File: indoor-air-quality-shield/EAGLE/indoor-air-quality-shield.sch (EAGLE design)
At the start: 36 parts, among them J4 POWER_JACKSLT, Q1 MMBT2222A, U6 AP1509-50SG-13

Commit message: upadted pcb layout
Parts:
- removed J4: POWER_JACKSLT, Spark:POWER_JACKSLT
- removed JP5: M02PTH3, SparkFun-Connectors:M02PTH3
- removed R13: 1K, SparkFun-Passives:RESISTOR0603-RES
- removed R14, R15: (no value), pot:TRIM_US-RJ9W
- added J3: (no value), Connector:TWIG-4P-2.0-2.0
- added JP2: (no value), SparkFun-Connectors:M03PTH
- added R7, R8, R9: 1K, SparkFun-Passives:RESISTOR0603-RES
- D1: value LED-RGB-CC-THRUCLEAR -> B230; device SparkFun-LED:LED-RGB-CC-THRUCLEAR -> adafruit:DIODESMA
- D3: value B230 -> LED-RGB-CC-THRUCLEAR; device adafruit:DIODESMA -> SparkFun-LED:LED-RGB-CC-THRUCLEAR
- J1: value (none) -> POWER_JACKSLT; device Connector:TWIG-4P-2.0-2.0 -> Spark:POWER_JACKSLT
- JP1: value (none) -> M02PTH3; device SparkFun-Connectors:M03PTH -> SparkFun-Connectors:M02PTH3
- R1, R2, R3, R4: value (none) -> 50K; device SparkFun-Passives:RESISTOR0603-RES -> pot:TRIM_US-RJ9W
- R10: value (none) -> 10K
- R11, R12: value (none) -> 10K; device pot:TRIM_US-RJ9W -> SparkFun-Passives:RESISTOR0603-RES
- R5, R6: value (none) -> 1K
- U$1: value SPARK_CORE -> MQ_SENSOR_SOCKET; device Spark:SPARK_CORE -> Spark:MQ_SENSOR_SOCKET
- U$3: value MICS5525 -> MQ_SENSOR_SOCKET; device Spark:MICS5525 -> Spark:MQ_SENSOR_SOCKET
- U$4: value MQ_SENSOR_SOCKET -> MICS5525; device Spark:MQ_SENSOR_SOCKET -> Spark:MICS5525
- U$5: value MQ_SENSOR_SOCKET -> DHT22; device Spark:MQ_SENSOR_SOCKET -> Spark:DHT22
- U$6: value DHT22 -> SPARK_CORE; device Spark:DHT22 -> Spark:SPARK_CORE
- renumbered C10 to C2, C8 to C3, C9 to C1, LED5 to LED1, R16 to R10, U6 to U1
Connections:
- net +3V3: now also U$5.VDD, U$6.3V3; no longer U$1.3V3, U$6.VDD
- net +5V: now also J3.3, R11.2, R12.2, U$1.A1, U$1.A2, U$1.H+, U$3.A1, U$3.A2, U$4.S+, U$6.VIN; no longer J1.3, R13.2, R4.2, U$1.VIN, U$3.S+, U$4.A1, U$4.A2, U$5.A1, U$5.A2, U$5.H+
- net BLUE: now also R7.2, U$6.A7; no longer R3.2, U$1.A7
- net BTN1: now also U$6.D3; no longer U$1.D3
- net BTN2: now also U$6.D4; no longer U$1.D4
- net BUZZER: now also U$6.A4
- net DHT22: now also U$5.DATA, U$6.D2; no longer U$1.D2, U$6.DATA
- net GND: now also D3.CATHODE, J1.GND, J1.GNDBREAK, J3.4, JP2.1, R1.A, R1.S, R2.A, R2.S, R3.A, R3.S, R4.A, R4.S, U$4.H-, U$5.GND, U$6.GND@2, U$6.GND@21; no longer D1.CATHODE, J1.4, J4.GND, J4.GNDBREAK, JP5.1, R11.A, R11.S, R12.A, R12.S, R14.A, R14.S, R15.A, R15.S, U$1.GND@2, U$1.GND@21, U$3.H-, U$6.GND
- net GREEN: now also R8.2, U$6.A6; no longer R2.2, U$1.A6
- net MICS: now also R3.E, U$4.S-, U$6.A1; no longer R12.E, U$1.A1, U$3.S-
- net MQ1: now also R2.E, U$1.B1, U$1.B2, U$6.A2; no longer R14.E, U$1.A2, U$4.B1, U$4.B2
- net MQ2: now also R4.E, U$3.B1, U$3.B2, U$6.A3; no longer R15.E, U$1.A3, U$5.B1, U$5.B2
- net N$1: now also D3.BLUE_CATHODE, R7.1; no longer D1.BLUE_CATHODE, R3.1
- net N$14: now also D1.C; no longer D3.C
- net N$16: now also R5.1; no longer R13.1
- net N$2: now also D3.GREEN_CATHODE, R8.1; no longer D1.GREEN_CATHODE, R2.1
- net N$3: now also D3.RED_CATHODE, R9.1; no longer D1.RED_CATHODE, R1.1
- net N$32: now also D1.A, J1.PWR, JP1.2; no longer D3.A, J4.PWR, JP5.2
- net RED: now also R9.2, U$6.A5; no longer R1.2, U$1.A5
- net SCL: now also J3.1, R11.1, U$6.D1; no longer J1.1, R4.1, U$1.D1
- net SDA: now also J3.2, R12.1, U$6.D0; no longer J1.2, R5.1, U$1.D0
- net TGS: now also R1.E, U$6.A0; no longer R11.E, U$1.A0
- net UART_RX: now also JP2.3, U$6.RX; no longer JP1.3, U$1.RX
- net UART_TX: now also JP2.2, U$6.TX; no longer JP1.2, U$1.TX
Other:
- moved on the sheet: R5

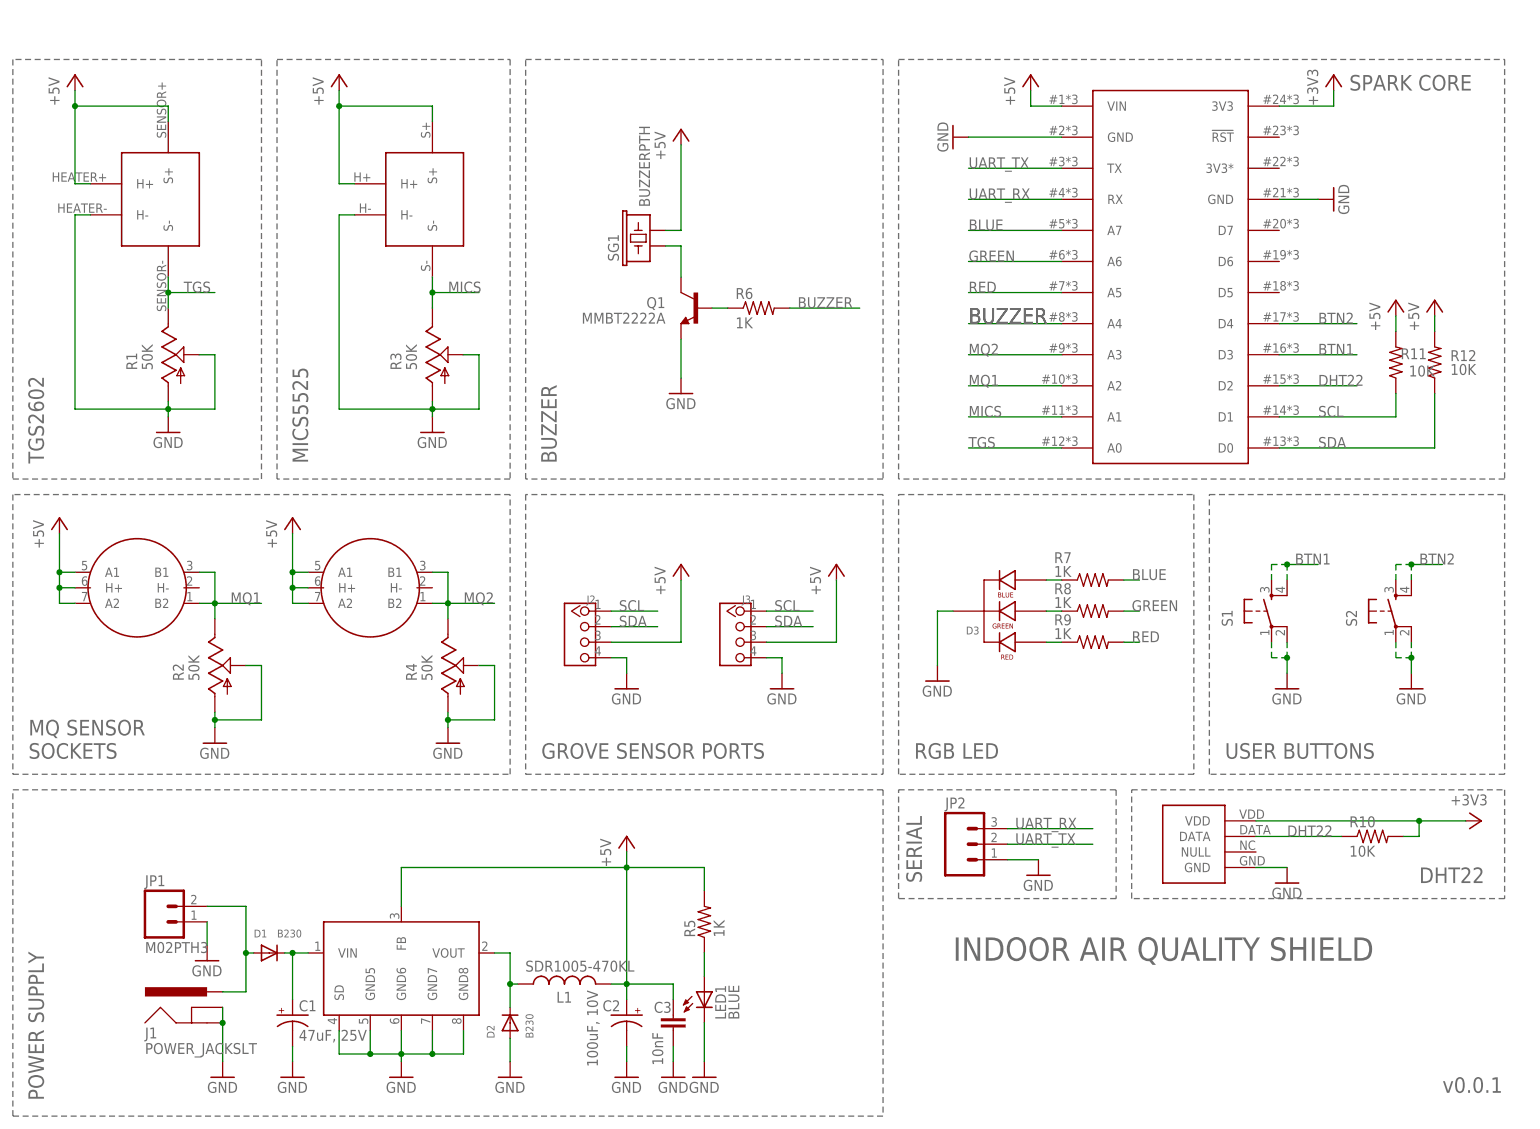
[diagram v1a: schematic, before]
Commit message: layed out indoor air quality pcb
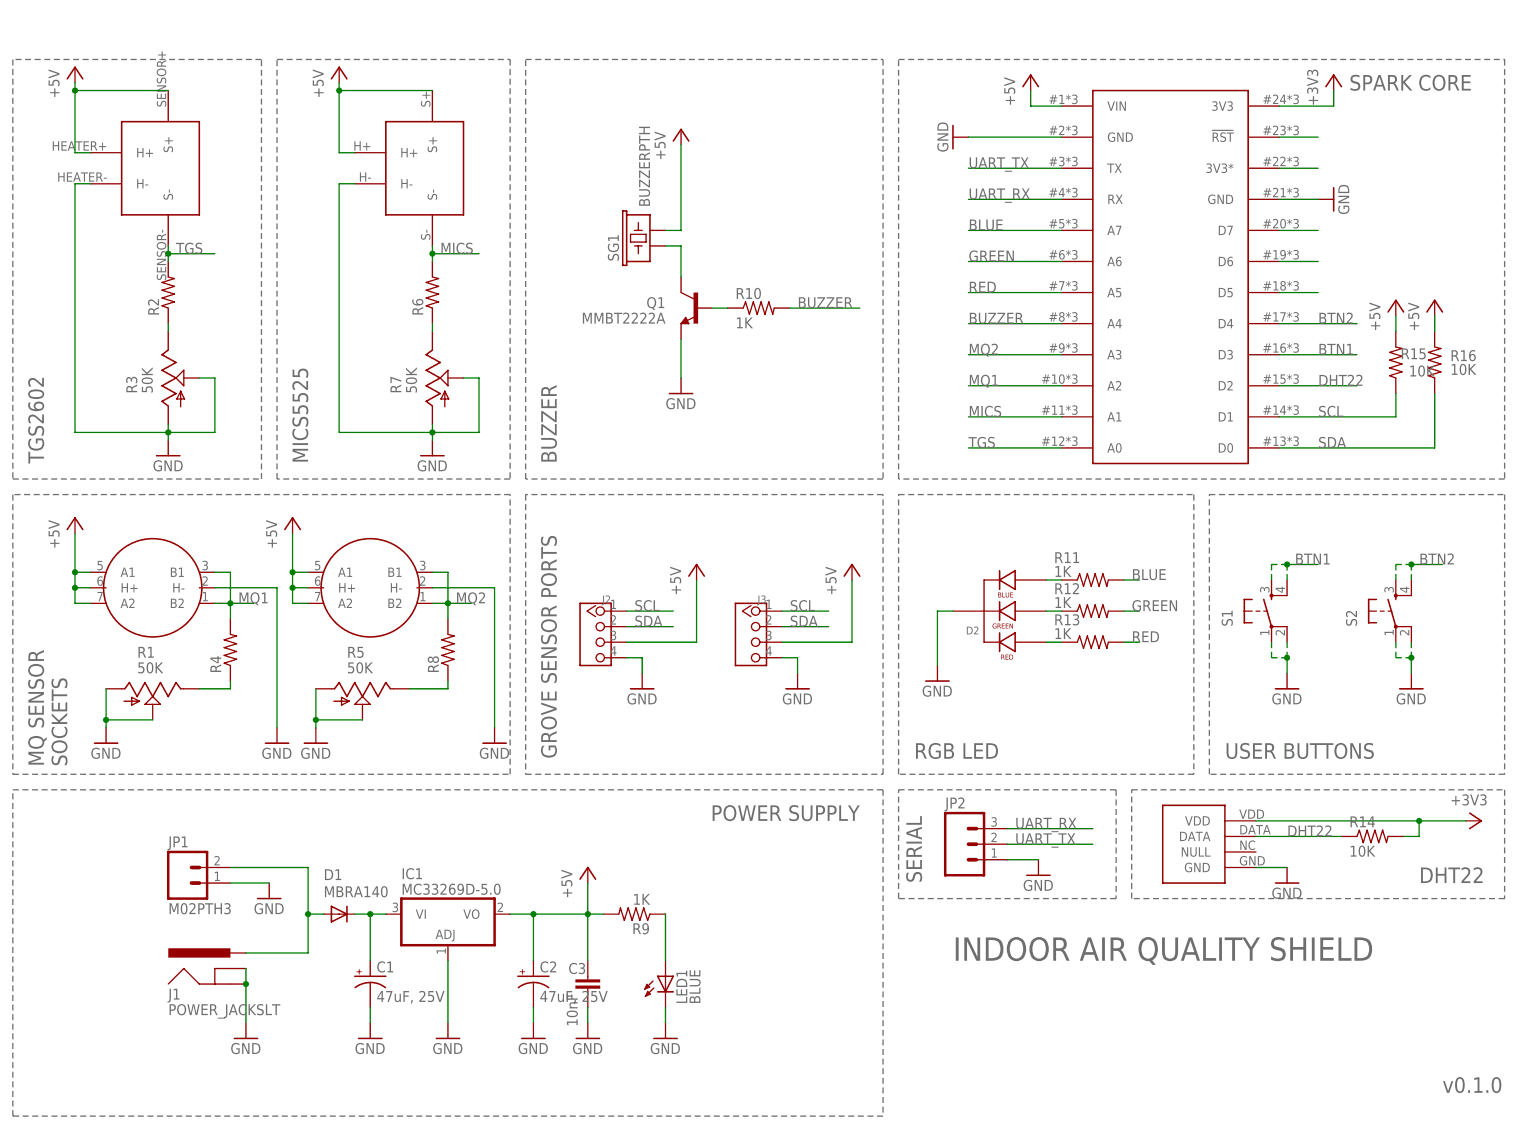
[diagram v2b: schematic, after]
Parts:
- removed D3: LED-RGB-CC-THRUCLEAR, SparkFun-LED:LED-RGB-CC-THRUCLEAR
- removed L1: SDR1005-470KL, Spark:INDUCTOR-SPARKFUN
- removed U1: AP1509-50SG-13, Spark:AP1509-50SG-13
- added IC1: MC33269D-5.0, linear:MC33269D-5.0
- added R13: 1K, SparkFun-Passives:RESISTOR0603-RES
- added R14, R15, R16: 10K, SparkFun-Passives:RESISTOR0603-RES
- C2: value 100uF, 10V -> 47uF, 25V
- D1: value B230 -> MBRA140; device adafruit:DIODESMA -> SparkFun-DiscreteSemi:DIODESMA
- D2: value B230 -> LED-RGB-CC-THRUCLEAR; device adafruit:DIODESMA -> SparkFun-LED:LED-RGB-CC-THRUCLEAR
- R10, R11, R12: value 10K -> 1K
- R2, R4: value 50K -> (none); device pot:TRIM_US-RJ9W -> SparkFun-Resistors:RESISTOR0603
- R5, R7: value 1K -> 50K; device SparkFun-Passives:RESISTOR0603-RES -> pot:TRIM_US-RJ9W
- R6, R8: value 1K -> (none); device SparkFun-Passives:RESISTOR0603-RES -> SparkFun-Resistors:RESISTOR0603
- U$1: value MQ_SENSOR_SOCKET -> TGS2602; device Spark:MQ_SENSOR_SOCKET -> Spark:TGS2602
- U$2: value TGS2602 -> MQ_SENSOR_SOCKET; device Spark:TGS2602 -> Spark:MQ_SENSOR_SOCKET
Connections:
- removed net N$14: C1.+, D1.C, U1.VIN
- removed net N$34: D2.C, L1.1, U1.VOUT
- new net N$10: R5.E, R8.1
- new net N$11: U$6.D7
- new net N$12: U$6.D6
- new net N$13: U$6.D5
- new net N$4: R2.1, R3.E
- new net N$5: U$6.!RST
- new net N$6: C1.+, D1.C, IC1.VI
- new net N$7: R6.1, R7.E
- new net N$8: R1.E, R4.1
- new net N$9: U$6.3V3*
- net +3V3: now also R14.2; no longer R10.2
- net +5V: now also IC1.VO, R15.2, R16.2, R9.2, U$1.S+, U$2.A1, U$2.A2; no longer L1.2, R11.2, R12.2, R5.2, U$1.A1, U$1.A2, U$2.S+, U1.FB
- net BLUE: now also R11.2; no longer R7.2
- net BUZZER: now also R10.2; no longer R6.2
- net DHT22: now also R14.1; no longer R10.1
- net GND: now also D2.CATHODE, IC1.ADJ, R5.A, R5.S, R7.A, R7.S, U$1.H-, U$3.H-; no longer D2.A, D3.CATHODE, R2.A, R2.S, R4.A, R4.S, U1.GND5, U1.GND6, U1.GND7, U1.GND8, U1.SD
- net GREEN: now also R12.2; no longer R8.2
- net MICS: now also R6.2; no longer R3.E
- net MQ1: now also R4.2, U$2.B1, U$2.B2; no longer R2.E, U$1.B1, U$1.B2
- net MQ2: now also R8.2; no longer R4.E
- net N$1: now also D2.BLUE_CATHODE, R11.1; no longer D3.BLUE_CATHODE, R7.1
- net N$15: now also R10.1; no longer R6.1
- net N$16: now also R9.1; no longer R5.1
- net N$2: now also D2.GREEN_CATHODE, R12.1; no longer D3.GREEN_CATHODE, R8.1
- net N$3: now also D2.RED_CATHODE, R13.1; no longer D3.RED_CATHODE, R9.1
- net RED: now also R13.2; no longer R9.2
- net SCL: now also R15.1; no longer R11.1
- net SDA: now also R16.1; no longer R12.1
- net TGS: now also R2.2, U$1.S-; no longer R1.E, U$2.S-
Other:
- note added: "v0.1.0"
- note removed: "v0.0.1"
- moved on the sheet: C1, C2, C3, D1, J1, J2, J3, JP1, LED1, R1, R10, R11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

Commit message: updated aq shield
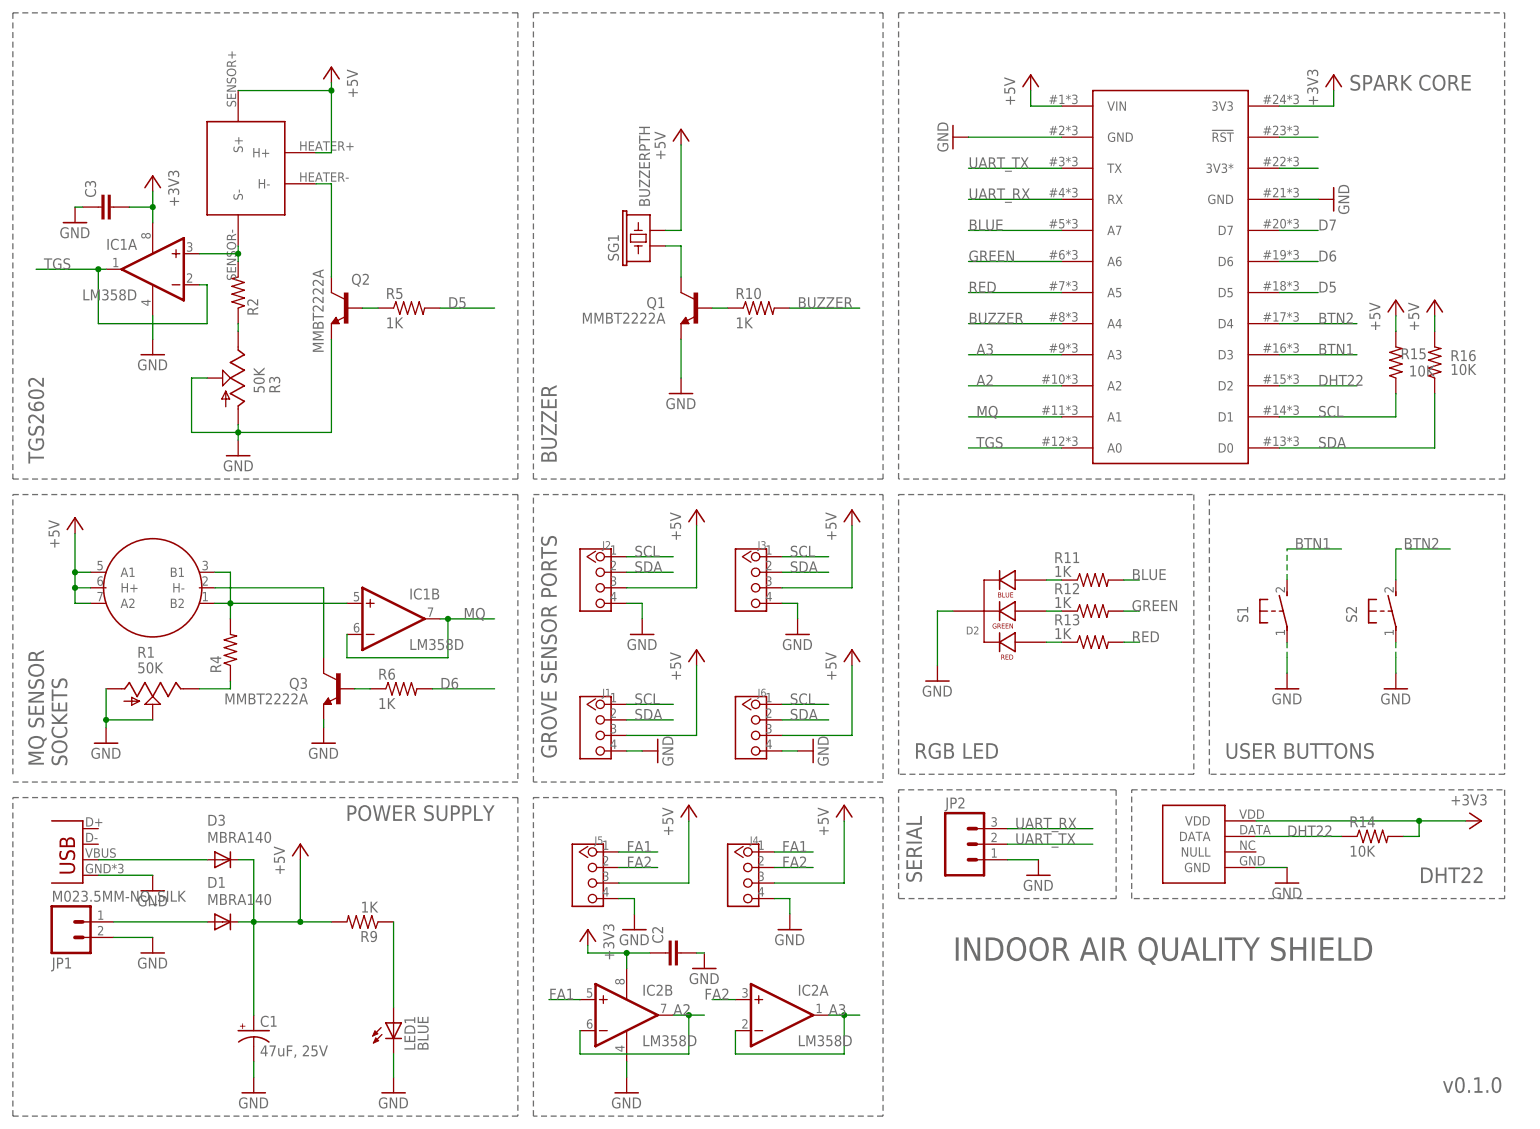
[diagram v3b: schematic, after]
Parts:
- removed R7: 50K, pot:TRIM_US-RJ9W
- removed R8: (no value), SparkFun-Resistors:RESISTOR0603
- removed U$3: MQ_SENSOR_SOCKET, Spark:MQ_SENSOR_SOCKET
- removed U$4: MICS5525, Spark:MICS5525
- added D3: MBRA140, SparkFun-DiscreteSemi:DIODESMA
- added IC2: LM358D, linear:LM358D
- added J4, J5, J6: (no value), Connector:TWIG-4P-2.0'D90'
- added JP3: USBUSB-MICROB-SLOT-HOLE, Spark:USBUSB-MICROB-SLOT-HOLE
- added Q2, Q3: MMBT2222A, SparkFun-DiscreteSemi:TRANSISTOR_NPNMMBT2222A
- C2: value 47uF, 25V -> (none); device SparkFun-Capacitors:CAP_POLD -> rcl:C-EUC0603
- C3: value 10nF -> (none); device SparkFun-Capacitors:CAP0603-CAP -> rcl:C-EUC0603
- IC1: value MC33269D-5.0 -> LM358D; device linear:MC33269D-5.0 -> linear:LM358D
- J1: value POWER_JACKSLT -> (none); device Spark:POWER_JACKSLT -> Connector:TWIG-4P-2.0'D90'
- J2, J3: device Connector:TWIG-4P-2.0-2.0 -> Connector:TWIG-4P-2.0'D90'
- JP1: value M02PTH3 -> M023.5MM-NO_SILK; device SparkFun-Connectors:M02PTH3 -> SparkFun-Connectors:M023.5MM-NO_SILK
- R5: value 50K -> 1K; device pot:TRIM_US-RJ9W -> SparkFun-Passives:RESISTOR0603-RES
- R6: value (none) -> 1K; device SparkFun-Resistors:RESISTOR0603 -> SparkFun-Passives:RESISTOR0603-RES
- S1, S2: device SparkFun-Electromechanical:TAC_SWITCHSMD -> switch-omron:31-XX
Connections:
- net N$11 renamed D7
- removed net MICS: R6.2, U$4.S-, U$6.A1
- removed net MQ1: R4.2, U$2.B1, U$2.B2, U$6.A2
- removed net MQ2: R8.2, U$3.B1, U$3.B2, U$6.A3
- removed net N$12: U$6.D6
- removed net N$13: U$6.D5
- removed net N$32: D1.A, J1.PWR, JP1.2
- new net A2: IC2B.-IN, IC2B.OUT, U$6.A2
- new net A3: IC2A.-IN, IC2A.OUT, U$6.A3
- new net D5: R5.2, U$6.D5
- new net D6: R6.2, U$6.D6
- new net FA1: IC2B.+IN, J4.1, J5.1
- new net FA2: IC2A.+IN, J4.2, J5.2
- new net MQ: IC1B.-IN, IC1B.OUT, U$6.A1
- new net N$11: IC1A.+IN, R2.2, U$1.S-
- new net N$14: Q3.B, R6.1
- new net N$18: Q2.C, U$1.H-
- new net N$19: Q2.B, R5.1
- new net N$23: IC1B.+IN, R4.2, U$2.B1, U$2.B2
- net +3V3: now also C2.1, C3.2, IC1P.V+, IC2P.V+
- net +5V: now also C1.+, D1.C, D3.C, J1.3, J4.3, J5.3, J6.3; no longer C2.+, C3.2, IC1.VO, U$3.A1, U$3.A2, U$3.H+, U$4.H+, U$4.S+
- net BTN1: now also S1.S; no longer S1.3, S1.4
- net BTN2: now also S2.S; no longer S2.3, S2.4
- net GND: now also C2.2, IC1P.V-, IC2P.V-, J1.4, J4.4, J5.4, J6.4, JP1.2, JP3.GND, Q2.E, Q3.E, S1.P, S2.P; no longer C2.-, IC1.ADJ, J1.GND, J1.GNDBREAK, JP1.1, R5.A, R5.S, R7.A, R7.S, S1.1, S1.2, S2.1, S2.2, U$1.H-, U$2.H-, U$3.H-, U$4.H-
- net N$10: now also D3.A, JP3.VBUS; no longer R5.E, R8.1
- net N$6: now also D1.A, JP1.1; no longer C1.+, D1.C, IC1.VI
- net N$7: now also Q3.C, U$2.H-; no longer R6.1, R7.E
- net SCL: now also J1.1, J6.1
- net SDA: now also J1.2, J6.2
- net TGS: now also IC1A.-IN, IC1A.OUT; no longer R2.2, U$1.S-
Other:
- note removed: "MICS5525"
- moved on the sheet: C1, C3, D1, J2, J3, JP1, LED1, R2, R3, R6, R9
